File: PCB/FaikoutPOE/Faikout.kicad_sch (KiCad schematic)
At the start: 91 parts, among them J1 RJ45_LED, J3 S21, J5 Reset, J7 TC2030-USB-NL-DS, M1 Ag9912-LP, P1 Square, P2 Square, P3 Square, P4 Square, P5 Square, P6 Square, P7 Square, P8 Square, Q1 BSS138PS, Q2 BSS138PS, U1 KSZ8851SNL, U2 ESP32-S3-MINI-1, U3 TCMT1100, U4 TPS62933, U5 TCMT1100, Y1 Crystal_GND24

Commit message: Tweak RJ45
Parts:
- J1: Position Offset 0,0.5 -> 0,0.4
- R14: MPN C158612 -> C473585
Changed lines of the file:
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@@
 			)
 		)
-		(property "MPN" "C158612"
+		(property "MPN" "C473585"
 			(at 199.39 31.75 0)
 			(hide yes)
@@
 			)
 		)
-		(property "Position Offset" "0,0.5"
+		(property "Position Offset" "0,0.4"
 			(at 33.02 151.13 0)
 			(hide yes)

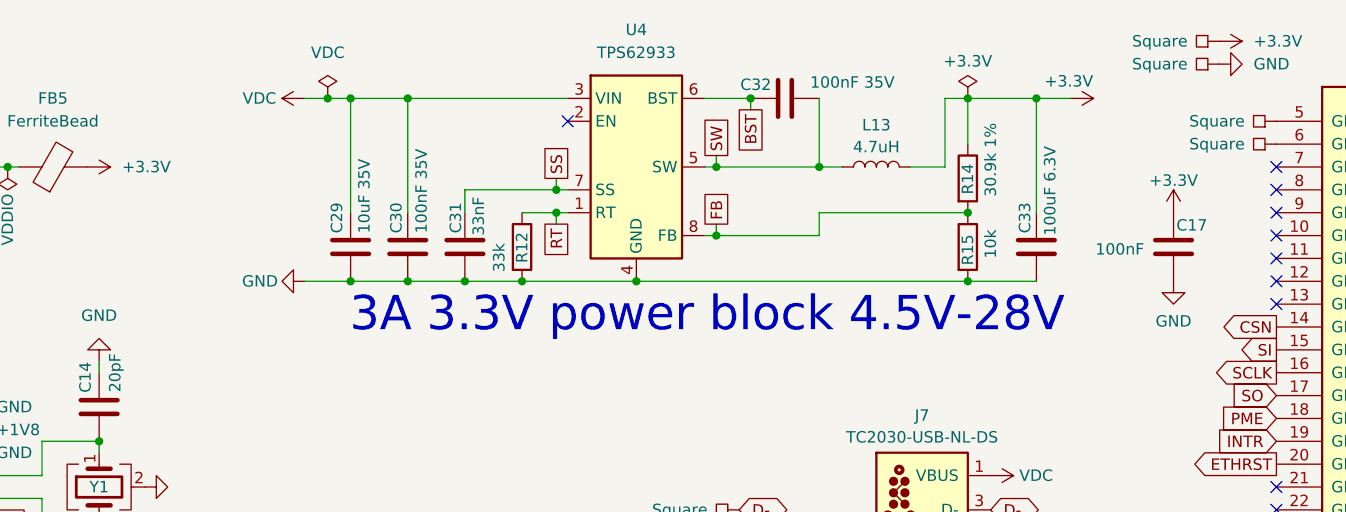
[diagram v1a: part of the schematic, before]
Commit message: New inductor
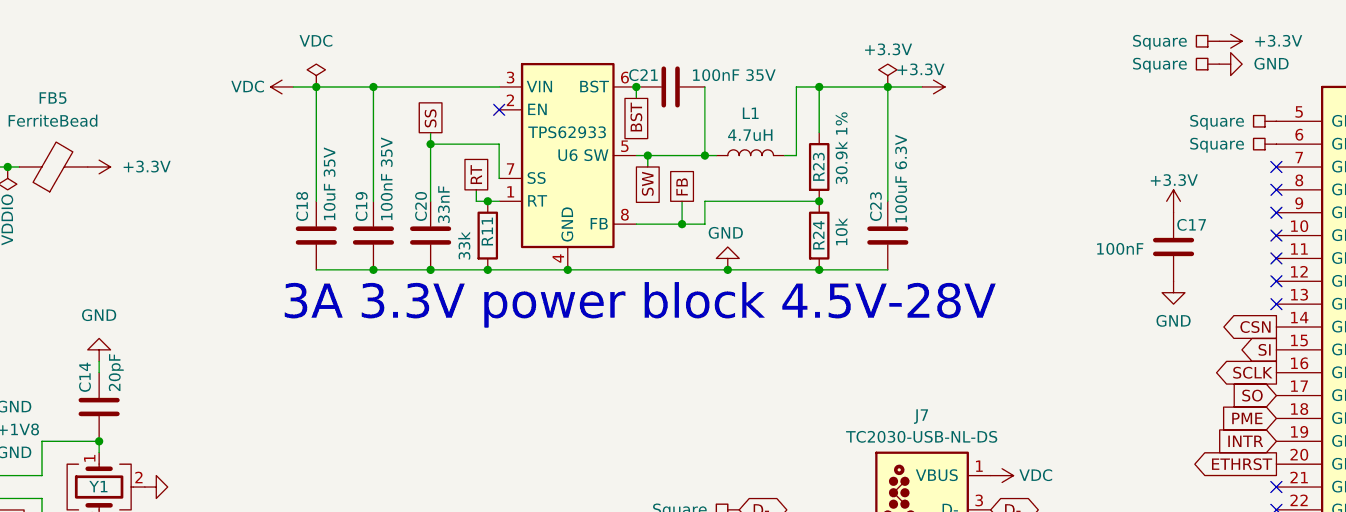
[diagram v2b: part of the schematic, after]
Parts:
- removed C29: 10uF 35V, RevK:C_0603, symbol Device:C
- removed C30, C32: 100nF 35V, RevK:C_0201, symbol Device:C
- removed C31: 33nF, RevK:C_0201, symbol Device:C
- removed C33: 100uF 6.3V, RevK:C_0805, symbol Device:C
- removed L13: 4.7uH, RevK:L_5x5, symbol Device:L
- removed R12: 33k, RevK:R_0201, symbol Device:R
- removed R14: 30.9k 1%, RevK:R_0201, symbol Device:R
- removed R15: 10k, RevK:R_0201, symbol Device:R
- removed U4: TPS62933, RevK:SOT-583-8, symbol Regulator_Switching:TPS62933
- added C18: 10uF 35V, RevK:C_0603, symbol Device:C
- added C19, C21: 100nF 35V, RevK:C_0201, symbol Device:C
- added C20: 33nF, RevK:C_0201, symbol Device:C
- added C23: 100uF 6.3V, RevK:C_0805, symbol Device:C
- added L1: 4.7uH, RevK:L_6x6, symbol Device:L
- added R11: 33k, RevK:R_0201, symbol Device:R
- added R23: 30.9k 1%, RevK:R_0201, symbol Device:R
- added R24: 10k, RevK:R_0201, symbol Device:R
- added U6: TPS62933, RevK:SOT-583-8, symbol Regulator_Switching:TPS62933
- M1: MPN C20564362 -> C6789853; now in the parts list
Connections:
- net +3.3V: now also C23.1, L1.2, R23.1
- net BST: now also C21.1, U6.6 (BST)
- net FB: now also R23.2, R24.1, U6.8 (FB)
- net GND: now also C18.2, C19.2, C20.2, C23.2, R11.2, R24.2, U6.4 (GND)
- net RT: now also R11.1, U6.1 (RT)
- net SS: now also C20.1, U6.7 (SS)
- net SW: now also C21.2, L1.1, U6.5 (SW)
- net VDC: now also C18.1, C19.1, U6.3 (VIN)
